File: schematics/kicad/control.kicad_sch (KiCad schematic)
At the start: 19 parts, among them U10 74F175, U1001 PAL20X10, U1002 PAL20X10, U1003 PAL20X10, U1004 PAL20R6, U1005 P16L8, U1006 PAL16R8, U1007 P16L8, U1008 P16L8, U1009 P16L8, U1010 P16L8, U1016 74F244, U1017 330Ω, U1036 330Ω, U1037 330Ω, U1038 330Ω, U5 PAL16R8, U6 330Ω

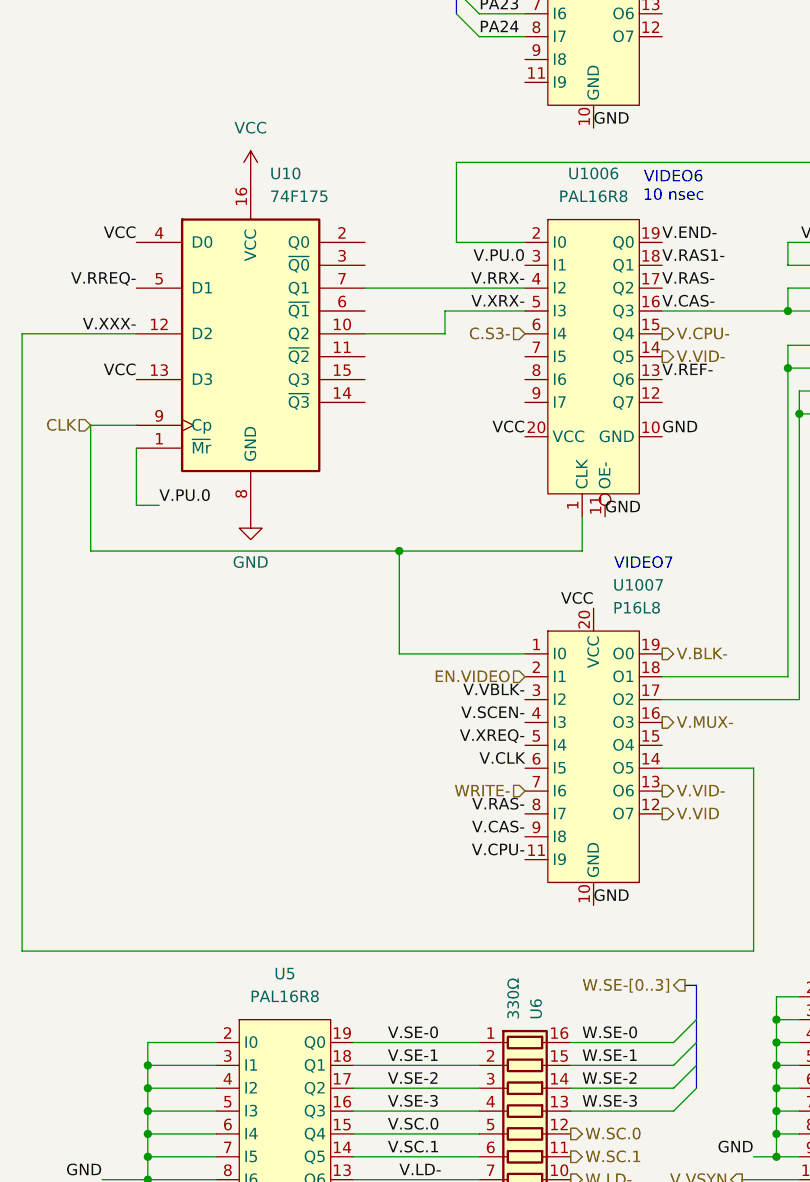
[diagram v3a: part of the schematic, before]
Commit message: First initial layout, fix ZIP footprint.
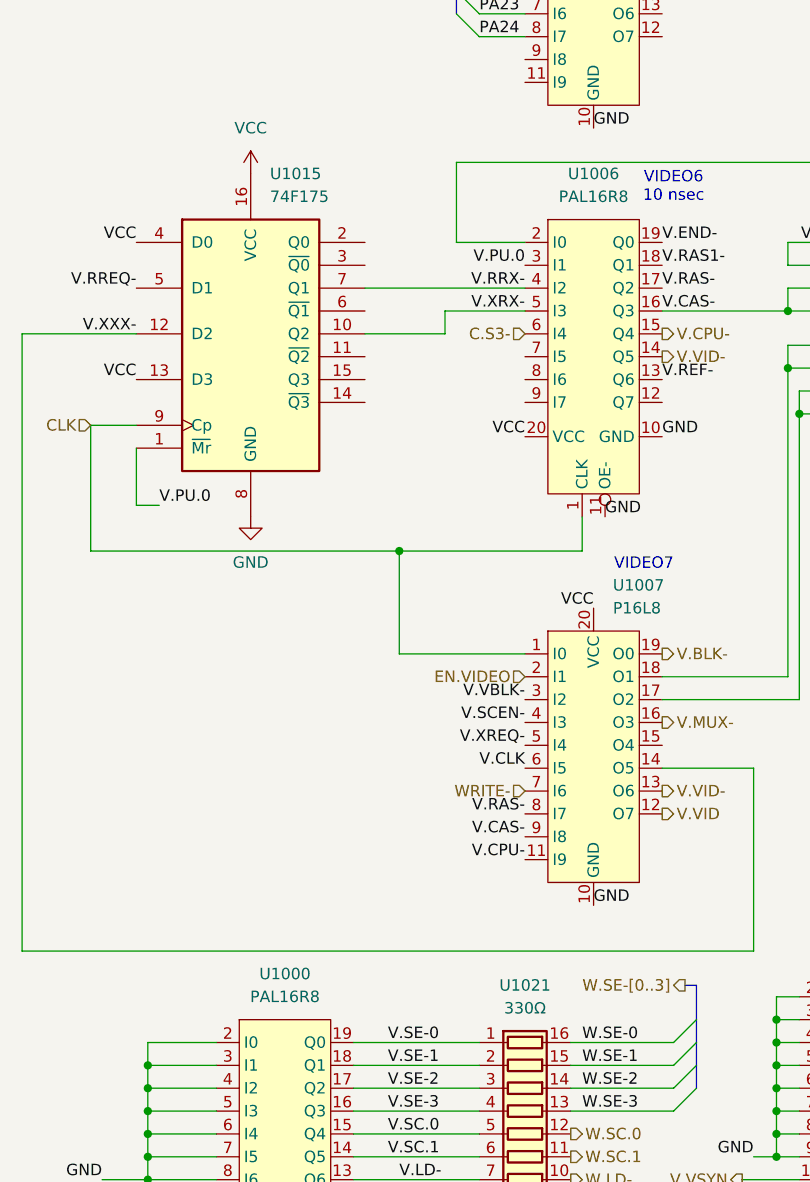
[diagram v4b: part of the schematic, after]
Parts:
- R7: footprint (none) -> Resistor_THT:R_Axial_DIN0207_L6.3mm_D2.5mm_P10.16mm_Horizontal
- renumbered U5 to U1000, U10 to U1015, U6 to U1021
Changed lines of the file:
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@@
 			)
 		)
-		(property "Footprint" ""
+		(property "Footprint" "Resistor_THT:R_Axial_DIN0207_L6.3mm_D2.5mm_P10.16mm_Horizontal"
 			(at 31.496 193.294 90)
 			(effects
@@
 		(dnp no)
 		(fields_autoplaced yes)
-		(property "Reference" "U10"
+		(property "Reference" "U1015"
 			(at 49.1333 57.15 0)
 			(effects
@@
 			(project ""
 				(path "/7c2b6a13-c303-4adb-8eed-6e6a9ac5307e/15921a63-59ee-470b-ba0e-36a85e35c802"
-					(reference "U10")
+					(reference "U1015")
 					(unit 1)
 				)
@@
 		(dnp no)
 		(fields_autoplaced yes)
-		(property "Reference" "U5"
+		(property "Reference" "U1000"
 			(at 50.8 146.05 0)
 			(effects
@@
 			(project "cg4"
 				(path "/7c2b6a13-c303-4adb-8eed-6e6a9ac5307e/15921a63-59ee-470b-ba0e-36a85e35c802"
-					(reference "U5")
+					(reference "U1000")
 					(unit 1)
 				)
@@
 		(dnp no)
 		(fields_autoplaced yes)
-		(property "Reference" "U6"
-			(at 78.7401 151.13 0)
-			(effects
-				(font
-					(size 1.27 1.27)
-				)
-				(justify right)
+		(property "Reference" "U1021"
+			(at 77.47 147.32 90)
+			(effects
+				(font
+					(size 1.27 1.27)
+				)
 			)
 		)
 		(property "Value" "330Ω"
-			(at 76.2001 151.13 0)
-			(effects
-				(font
-					(size 1.27 1.27)
-				)
-				(justify right)
+			(at 77.47 149.86 90)
+			(effects
+				(font
+					(size 1.27 1.27)
+				)
 			)
 		)
@@
 			(project "cg4"
 				(path "/7c2b6a13-c303-4adb-8eed-6e6a9ac5307e/15921a63-59ee-470b-ba0e-36a85e35c802"
-					(reference "U6")
-					(unit 1)
-				)
+					(reference "U1021")
+					(unit 1)
+				)

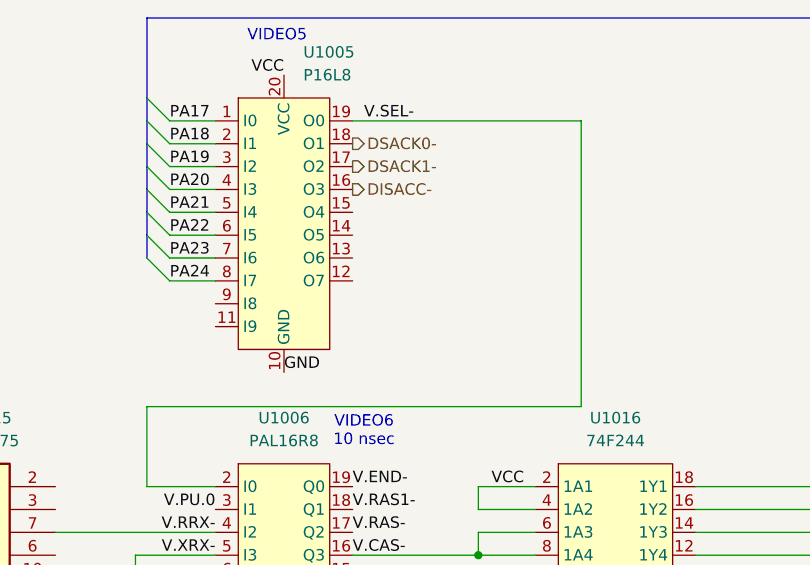
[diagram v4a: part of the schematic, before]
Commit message: Fix layout of the memory chips based on the board Fix the orientation of the P4 connector Connect CS.DAC- based on the board Change the orientation of the ECL resistors to route better Fix the copper islands to match the board, only DAC is on analog island, ECL and crystal are separate. Fix ECL VCC to VCC Confirm VEE not used Add PALs - U1000 missing
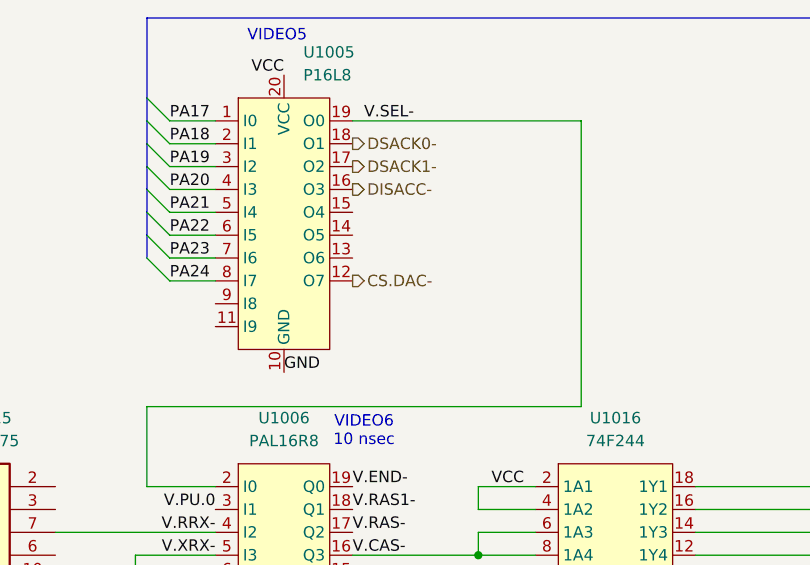
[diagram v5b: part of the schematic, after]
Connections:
- net CS.DAC-: now reaches U1005.12 (O7)
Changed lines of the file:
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@@
+		)
+	)
+	(hierarchical_label "CS.DAC-"
+		(shape output)
+		(at 92.71 41.91 0)
+		(effects
+			(font
+				(size 1.27 1.27)
+			)
+			(justify left)
 		)
 	)

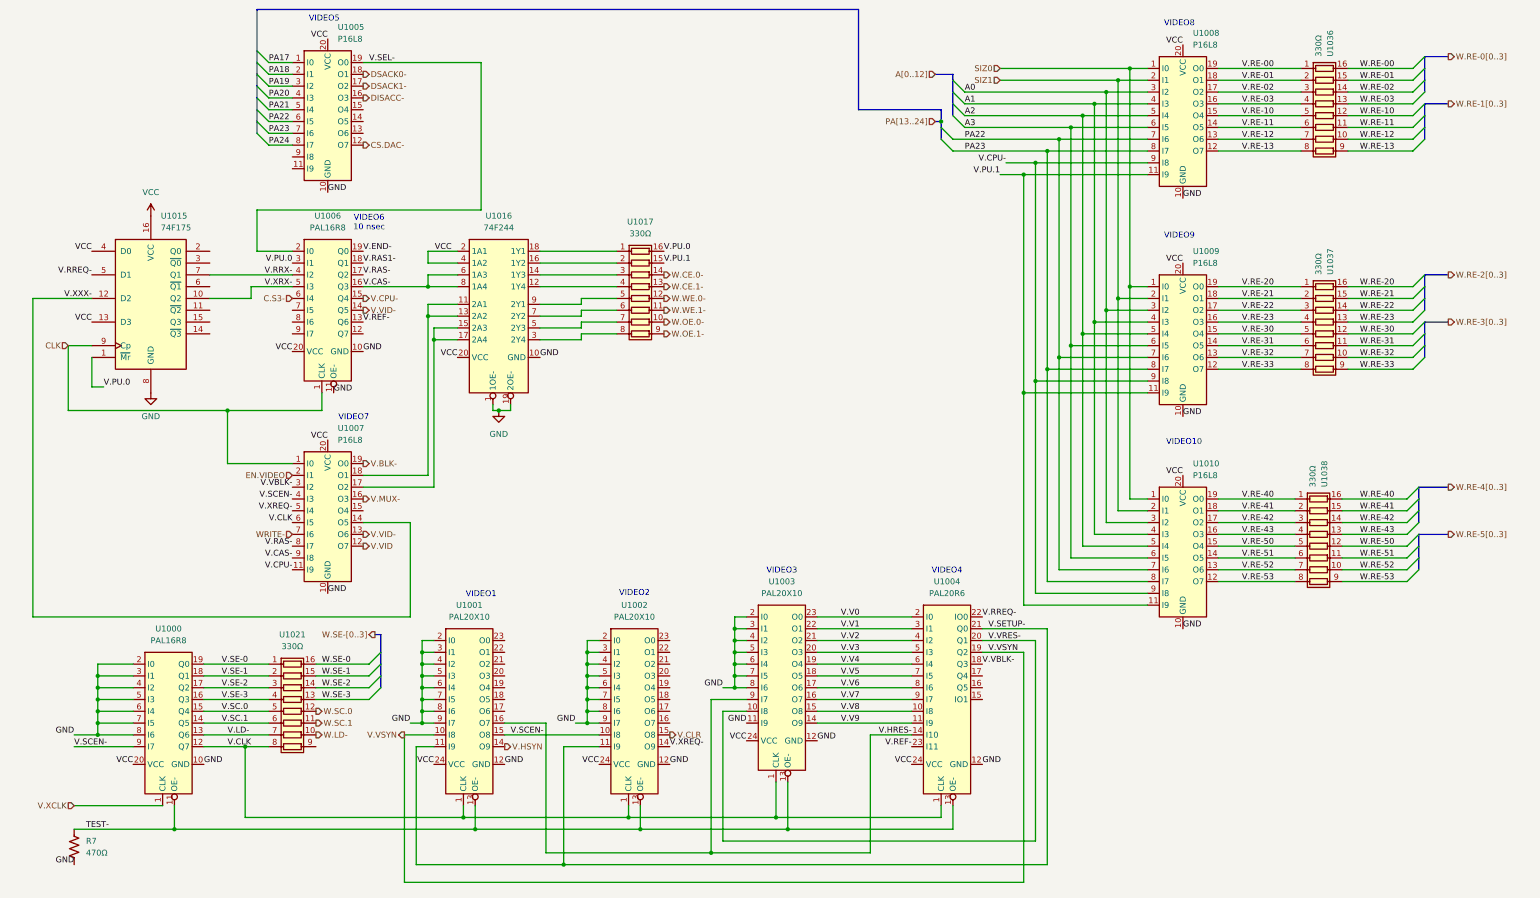
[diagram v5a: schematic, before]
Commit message: Fix the schematics as per the tracing of the actual board. fork a layout with the original positioning. New version PCB that should make routing easier.
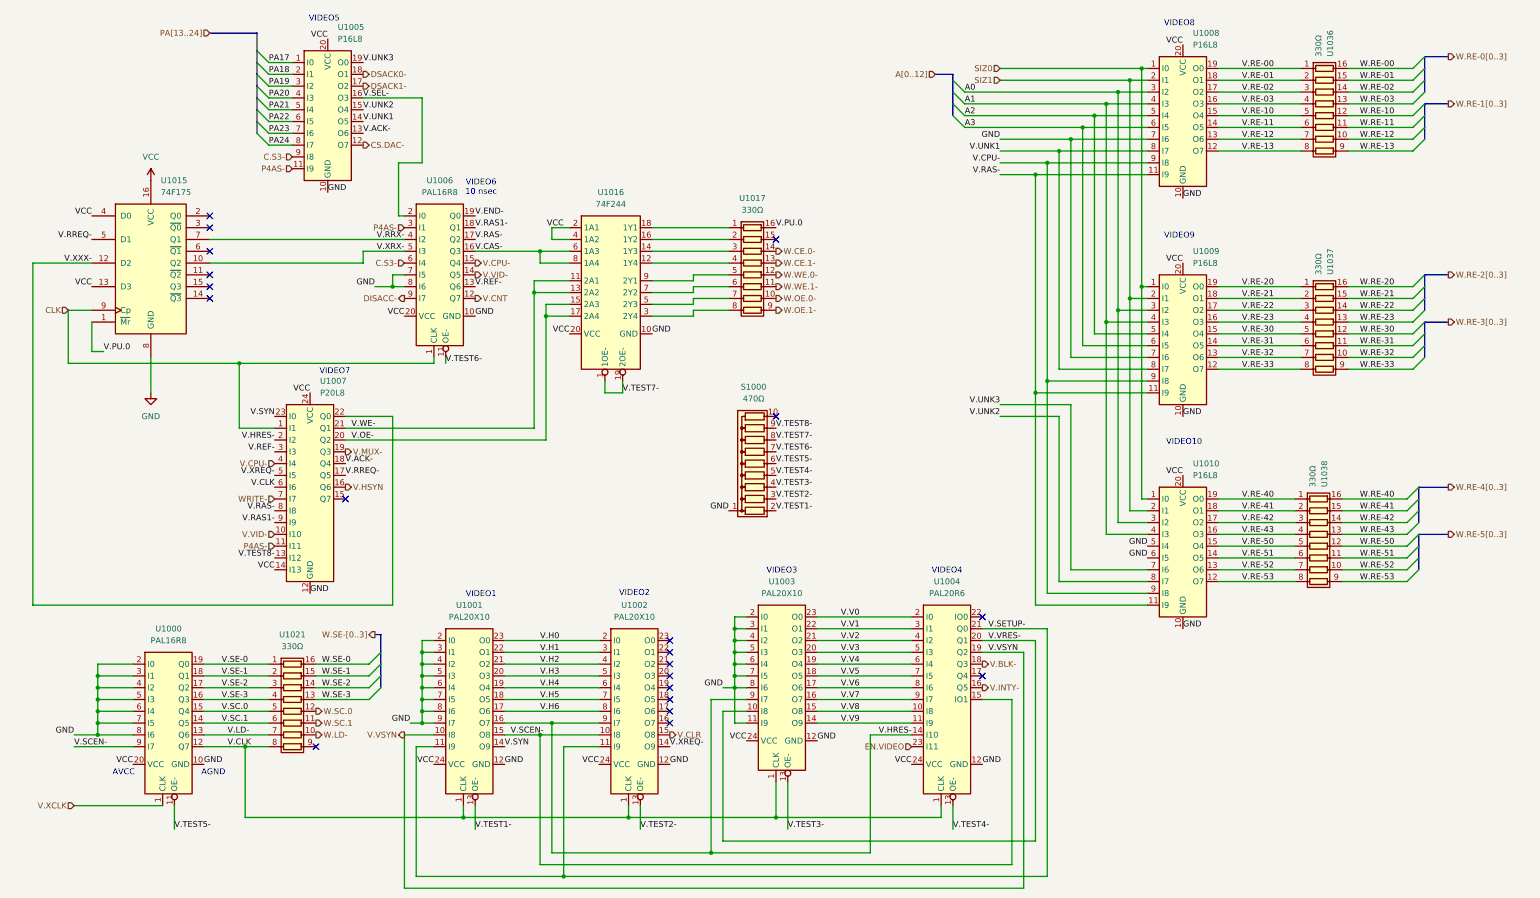
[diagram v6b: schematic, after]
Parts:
- removed R7: 470Ω, Resistor_THT:R_Axial_DIN0207_L6.3mm_D2.5mm_P10.16mm_Horizontal, symbol Device:R_US
- removed U1007: P16L8, Package_DIP:DIP-20_W7.62mm, symbol cg4:P16L8
- added S1000: 470Ω, Resistor_THT:R_Array_SIP10, symbol Device:R_Network09
- added U1007: P20L8, Package_DIP:DIP-24_W7.62mm, symbol cg4:P20L8
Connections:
- net V.VBLK- is gone; now on net V.BLK-: U1004.18 (Q3)
- net A2: no longer U1010.5 (I4)
- net A3: no longer U1010.6 (I5)
- net C.S3-: now also U1005.9 (I8)
- net CLK: now also U1007.1 (I1)
- net DISACC-: now also U1006.9 (I7); no longer U1005.16 (O3)
- net EN.VIDEO: now also U1004.23 (I11)
- net GND: now also U1006.7 (I5), U1006.8 (I6), U1008.7 (I6), U1009.7 (I6), U1010.5 (I4), U1010.6 (I5), S1000.1 (common), U1007.12 (GND); no longer U1002.2 (I0), U1002.3 (I1), U1002.4 (I2), U1002.5 (I3), U1002.6 (I4), U1002.7 (I5), U1002.8 (I6), U1002.9 (I7), U1006.11 (OE-), U1016.1 (1OE-), U1016.19 (2OE-)
- net PA22: no longer U1008.7 (I6), U1009.7 (I6), U1010.7 (I6)
- net PA23: no longer U1008.8 (I7), U1009.8 (I7), U1010.8 (I7)
- net V.CLK: now also U1007.6 (I6)
- net V.CPU-: now also U1007.4 (I4)
- net V.HRES-: now also U1002.9 (I7), U1007.2 (I2)
- net V.HSYN: now also U1007.16 (Q6); no longer U1001.14 (O9)
- net V.MUX-: now also U1007.19 (Q3)
- net V.PU.0: no longer U1006.3 (I1)
- net V.RAS-: now also U1008.11 (I9), U1009.11 (I9), U1010.11 (I9), U1007.8 (I8)
- net V.RAS1-: now also U1007.9 (I9)
- net V.REF-: now also U1007.3 (I3); no longer U1004.23 (I11)
- net V.RREQ-: now also U1007.17 (Q5); no longer U1004.22 (IO0)
- net V.SCEN-: now also U1004.15 (IO1)
- net V.SEL-: now also U1005.16 (O3); no longer U1005.19 (O0)
- net V.VID-: now also U1007.10 (I10)
- net V.XREQ-: now also U1007.5 (I5)
- net V.XXX-: now also U1007.22 (Q0)
- net VCC: now also U1007.14 (I13), U1007.24 (VCC)
- net WRITE-: now also U1007.7 (I7)
- net P4AS-: now reaches U1005.11 (I9)
- net P4AS-: now also U1006.3 (I1), U1007.11 (I11)
- net V.ACK-: now reaches U1005.13 (O6)
- net V.ACK-: now also U1007.18 (Q4)
- net V.UNK1: now reaches U1005.14 (O5)
- net V.UNK1: now also U1008.8 (I7), U1009.8 (I7)
- net V.UNK2: now reaches U1005.15 (O4)
- net V.UNK2: now also U1010.8 (I7)
- net V.INTY-: now reaches U1004.16 (Q5)
- net V.H6: now reaches U1001.17 (O6)
- net V.H6: now also U1002.8 (I6)
- net V.H5: now reaches U1001.18 (O5)
- net V.H5: now also U1002.7 (I5)
- net V.H4: now reaches U1001.19 (O4)
- net V.H4: now also U1002.6 (I4)
- net V.H3: now reaches U1001.20 (O3)
- net V.H3: now also U1002.5 (I3)
- net V.H2: now reaches U1001.21 (O2)
- net V.H2: now also U1002.4 (I2)
- net V.H1: now reaches U1001.22 (O1)
- net V.H1: now also U1002.3 (I1)
- net V.H0: now reaches U1001.23 (O0)
- net V.H0: now also U1002.2 (I0)
- net V.OE-: now reaches U1016.15 (2A3), U1016.17 (2A4)
- net V.OE-: now also U1007.20 (Q2)
- net V.WE-: now reaches U1016.11 (2A1), U1016.13 (2A2)
- net V.WE-: now also U1007.21 (Q1)
- net V.CNT: now reaches U1006.12 (Q7)
- removed net TEST-: U1000.11 (OE-), U1001.13 (OE-), U1002.13 (OE-), U1003.13 (OE-), U1004.13 (OE-)
- removed net V.PU.1: U1008.11 (I9), U1009.11 (I9), U1010.11 (I9), U1017.15 (R2.2)
- new net V.SYN: U1001.14 (O9), U1007.23 (I0)
- new net V.TEST1-: S1000.2 (R1), U1001.13 (OE-)
- new net V.TEST2-: S1000.3 (R2), U1002.13 (OE-)
- new net V.TEST3-: S1000.4 (R3), U1003.13 (OE-)
- new net V.TEST4-: S1000.5 (R4), U1004.13 (OE-)
- new net V.TEST5-: S1000.6 (R5), U1000.11 (OE-)
- new net V.TEST6-: S1000.7 (R6), U1006.11 (OE-)
- new net V.TEST7-: S1000.8 (R7), U1016.1 (1OE-), U1016.19 (2OE-)
- new net V.TEST8-: S1000.9 (R8), U1007.13 (I12)
- new net V.UNK3: U1005.19 (O0), U1010.7 (I6)
- no-connect marks 0 -> 20
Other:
- note added: "AGND"
- note added: "AVCC"
- moved on the sheet: U1006, U1015, U1016, U1017
